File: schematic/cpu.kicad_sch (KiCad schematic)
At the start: 3 parts, among them U1 Z80CPU

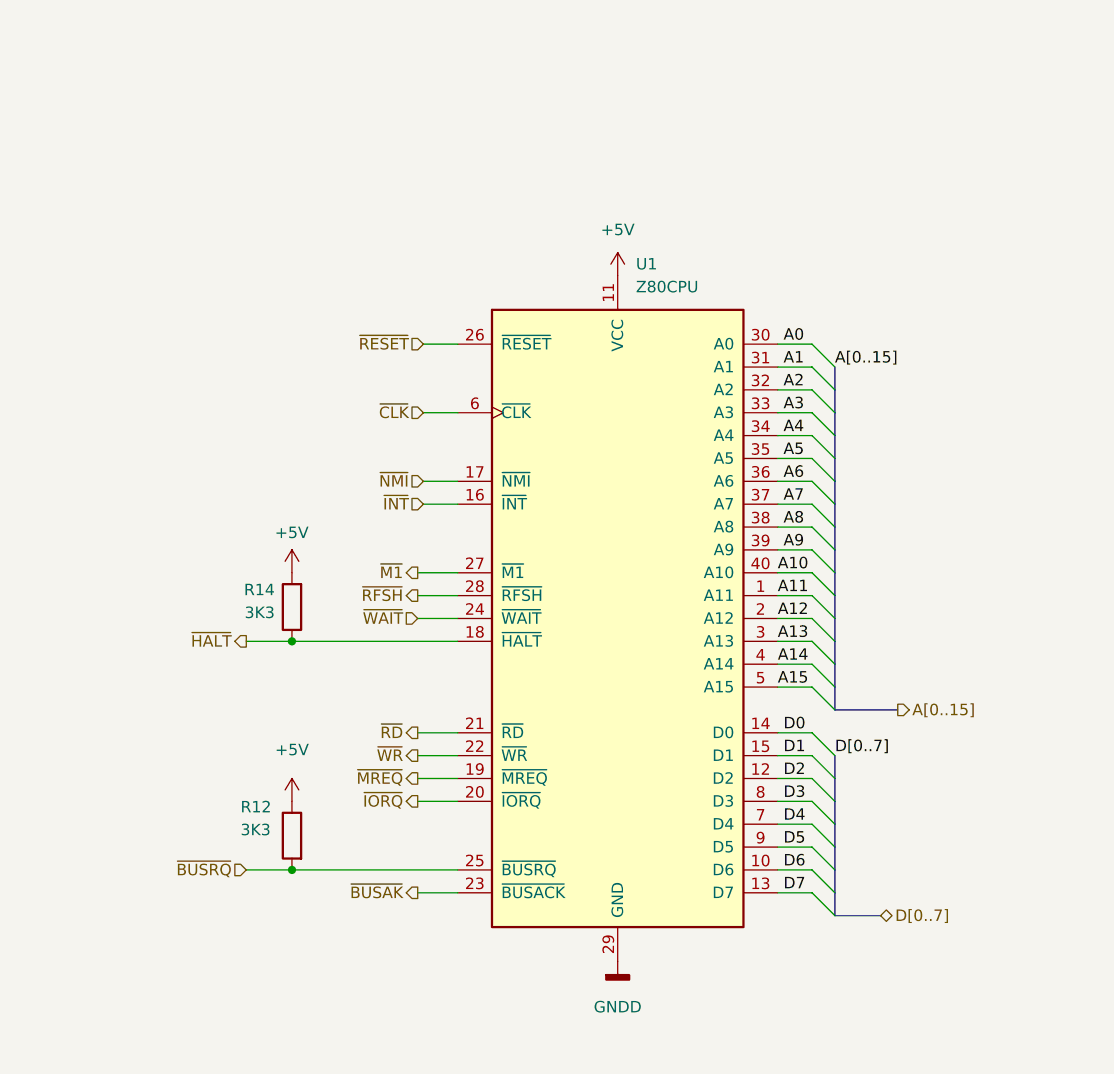
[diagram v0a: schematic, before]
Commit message: first commit of portable coleco, major changes... pcb meh. CPLD code tested, quartus build works.
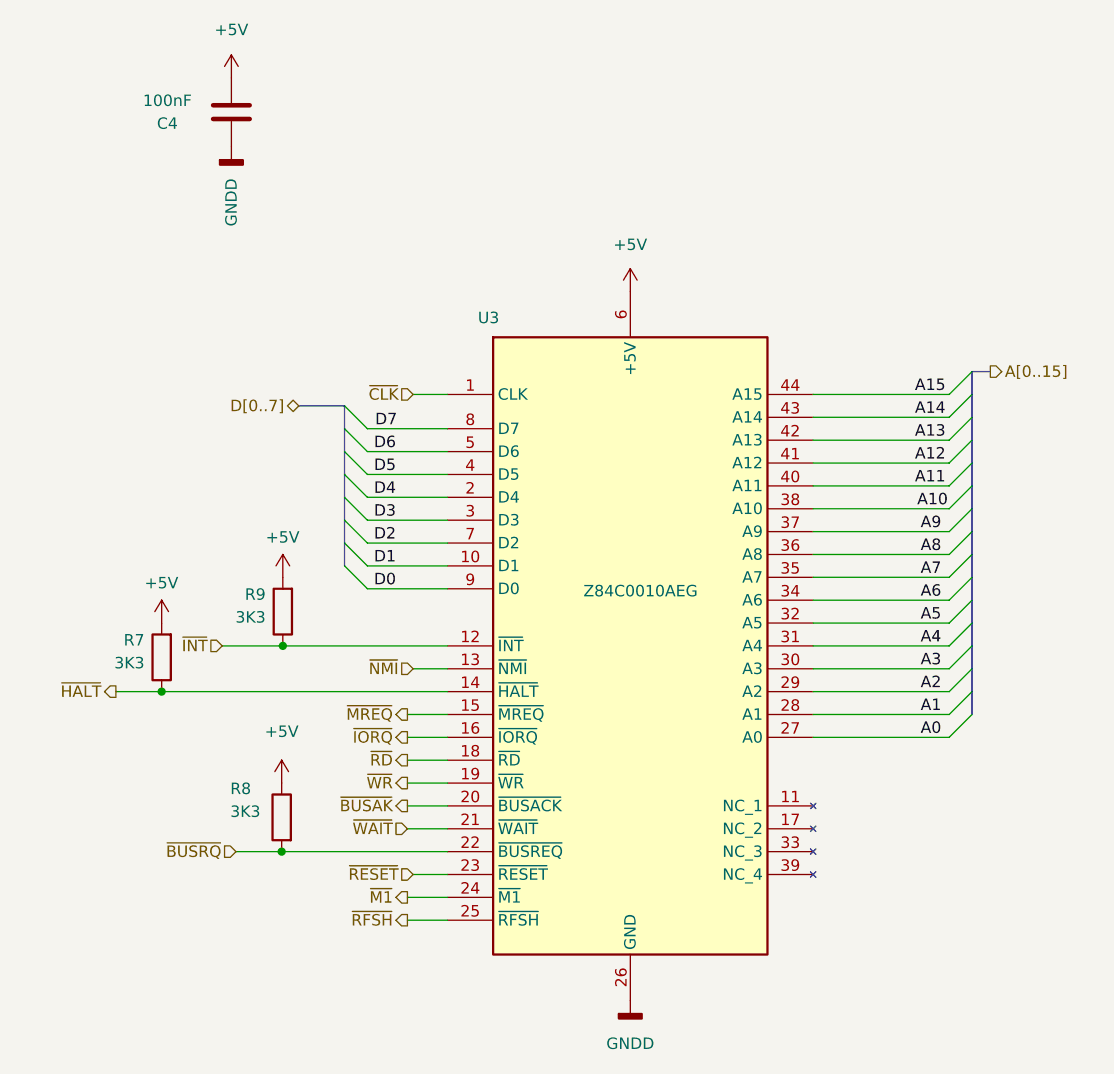
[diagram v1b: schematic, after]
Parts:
- removed U1: Z80CPU, Package_DIP:DIP-40_W15.24mm_LongPads, symbol CPU:Z80CPU
- added C4: 100nF, Capacitor_THT:C_Disc_D7.0mm_W2.5mm_P5.00mm, symbol Device:C
- added R9: 3K3, Resistor_THT:R_Axial_DIN0207_L6.3mm_D2.5mm_P10.16mm_Horizontal, symbol Device:R
- added U3: Z84C0010AEG, Package_QFP:LQFP-44_10x10mm_P0.8mm, symbol CPU_EXT:Z84C0010AEG
- renumbered R14 to R7, R12 to R8
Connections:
- net +5V: now also C4.1, R9.2, U3.6 (+5V)
- net A0: now also U3.27 (A0)
- net A1: now also U3.28 (A1)
- net A10: now also U3.38 (A10)
- net A11: now also U3.40 (A11)
- net A12: now also U3.41 (A12)
- net A13: now also U3.42 (A13)
- net A14: now also U3.43 (A14)
- net A15: now also U3.44 (A15)
- net A2: now also U3.29 (A2)
- net A3: now also U3.30 (A3)
- net A4: now also U3.31 (A4)
- net A5: now also U3.32 (A5)
- net A6: now also U3.34 (A6)
- net A7: now also U3.35 (A7)
- net A8: now also U3.36 (A8)
- net A9: now also U3.37 (A9)
- net D0: now also U3.9 (D0)
- net D1: now also U3.10 (D1)
- net D2: now also U3.7 (D2)
- net D3: now also U3.3 (D3)
- net D4: now also U3.2 (D4)
- net D5: now also U3.4 (D5)
- net D6: now also U3.5 (D6)
- net D7: now also U3.8 (D7)
- net GNDD: now also C4.2, U3.26 (GND)
- net ~{BUSAK}: now also U3.20 (~{BUSACK})
- net ~{BUSRQ}: now also U3.22 (~{BUSREQ})
- net ~{CLK}: now also U3.1 (CLK)
- net ~{HALT}: now also U3.14 (~{HALT})
- net ~{INT}: now also R9.1, U3.12 (~{INT})
- net ~{IORQ}: now also U3.16 (~{IORQ})
- net ~{M1}: now also U3.24 (~{M1})
- net ~{MREQ}: now also U3.15 (~{MREQ})
- net ~{NMI}: now also U3.13 (~{NMI})
- net ~{RD}: now also U3.18 (~{RD})
- net ~{RESET}: now also U3.23 (~{RESET})
- net ~{RFSH}: now also U3.25 (~{RFSH})
- net ~{WAIT}: now also U3.21 (~{WAIT})
- net ~{WR}: now also U3.19 (~{WR})
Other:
- moved on the sheet: R7, R8

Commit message: first prototype board complete with smd ram
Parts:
- C4: footprint Capacitor_THT:C_Disc_D7.0mm_W2.5mm_P5.00mm -> Capacitor_SMD:C_1206_3216Metric
- R7, R8, R9: footprint Resistor_THT:R_Axial_DIN0207_L6.3mm_D2.5mm_P10.16mm_Horizontal -> Resistor_SMD:R_0805_2012Metric
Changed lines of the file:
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@@
       (effects (font (size 1.27 1.27)) (justify right))
     )
-    (property "Footprint" "Resistor_THT:R_Axial_DIN0207_L6.3mm_D2.5mm_P10.16mm_Horizontal" (at 104.14 116.078 90)
+    (property "Footprint" "Resistor_SMD:R_0805_2012Metric" (at 104.14 116.078 90)
       (effects (font (size 1.27 1.27)) hide)
     )
@@
       (effects (font (size 1.27 1.27)))
     )
-    (property "Footprint" "Capacitor_THT:C_Disc_D7.0mm_W2.5mm_P5.00mm" (at 97.7392 41.529 0)
+    (property "Footprint" "Capacitor_SMD:C_1206_3216Metric" (at 97.7392 41.529 0)
       (effects (font (size 1.27 1.27)) hide)
     )
@@
       (effects (font (size 1.27 1.27)) (justify left))
     )
-    (property "Footprint" "Resistor_THT:R_Axial_DIN0207_L6.3mm_D2.5mm_P10.16mm_Horizontal" (at 90.805 98.298 90)
+    (property "Footprint" "Resistor_SMD:R_0805_2012Metric" (at 90.805 98.298 90)
       (effects (font (size 1.27 1.27)) hide)
     )
@@
       (effects (font (size 1.27 1.27)) (justify left))
     )
-    (property "Footprint" "Resistor_THT:R_Axial_DIN0207_L6.3mm_D2.5mm_P10.16mm_Horizontal" (at 104.267 93.218 90)
-      (effects (font (size 1.27 1.27)) hide)
-    )
+    (property "Footprint" "Resistor_SMD:R_0805_2012Metric" (at 104.267 93.218 90)
+      (effects (font (size 1.27 1.27)) hide)
+    )

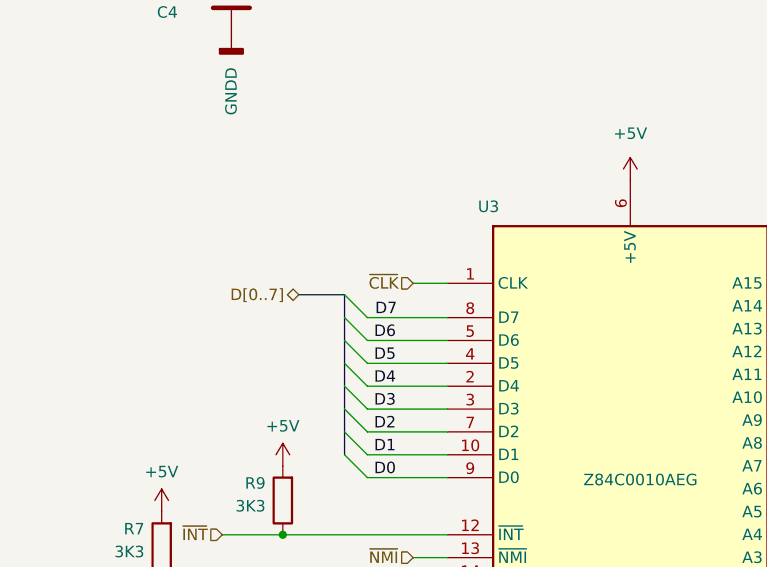
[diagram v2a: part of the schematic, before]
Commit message: added power port for lcd and adjusted board traces and fill
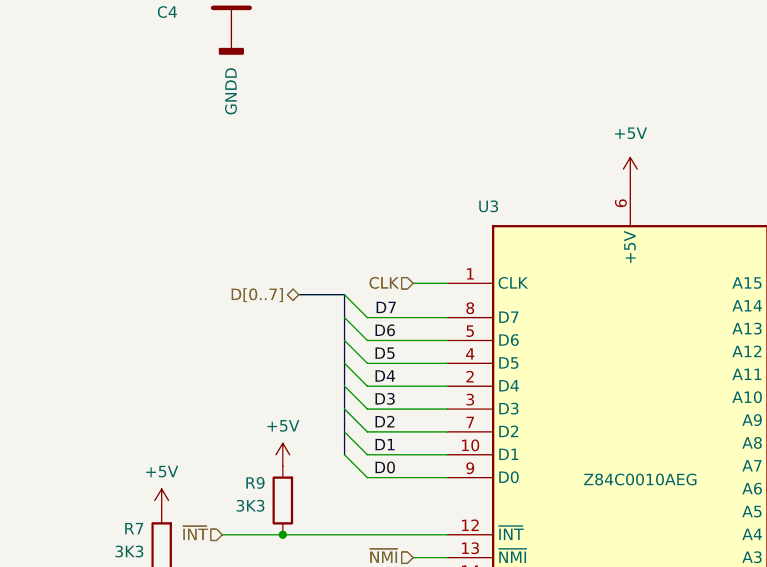
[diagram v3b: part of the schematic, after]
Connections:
- net ~{CLK} renamed CLK
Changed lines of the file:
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@@
     (effects (font (size 1.27 1.27)) (justify left))
   )
-  (hierarchical_label "~{CLK}" (shape input) (at 116.967 69.088 180) (fields_autoplaced)
+  (hierarchical_label "CLK" (shape input) (at 116.967 69.088 180) (fields_autoplaced)
     (effects (font (size 1.27 1.27)) (justify right))
   )

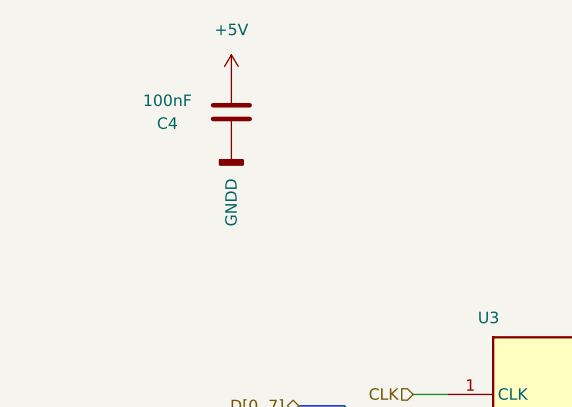
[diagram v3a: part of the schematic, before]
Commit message: first version with roller controller compat
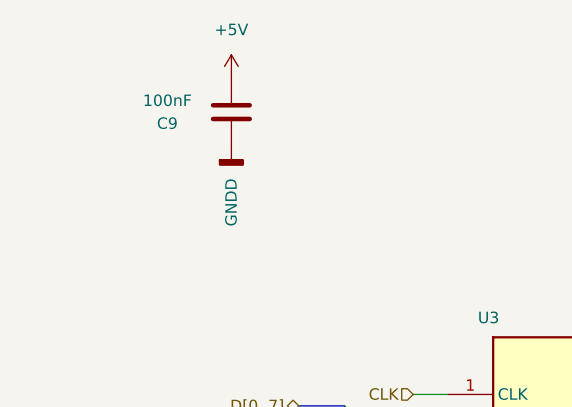
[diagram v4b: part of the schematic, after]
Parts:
- renumbered C4 to C9
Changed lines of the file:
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@@
   (symbol (lib_id "power:+5V") (at 96.774 33.909 0) (unit 1)
     (in_bom yes) (on_board yes) (dnp no) (fields_autoplaced)
-    (property "Reference" "#PWR021" (at 96.774 37.719 0)
+    (property "Reference" "#PWR018" (at 96.774 37.719 0)
       (effects (font (size 1.27 1.27)) hide)
     )
@@
     (instances
       (project "coleco_original"
-        (path "/970e0f64-111f-41e3-9f5a-fb0d0f6fa101/00000000-0000-0000-0000-00006262cd34"
-          (reference "#PWR021") (unit 1)
-        )
         (path "/970e0f64-111f-41e3-9f5a-fb0d0f6fa101/00000000-0000-0000-0000-00006262471e"
           (reference "#PWR018") (unit 1)
@@
   (symbol (lib_id "power:GNDD") (at 96.774 41.529 0) (unit 1)
     (in_bom yes) (on_board yes) (dnp no)
-    (property "Reference" "#PWR022" (at 96.774 47.879 0)
+    (property "Reference" "#PWR019" (at 96.774 47.879 0)
       (effects (font (size 1.27 1.27)) hide)
     )
@@
     (instances
       (project "coleco_original"
-        (path "/970e0f64-111f-41e3-9f5a-fb0d0f6fa101/00000000-0000-0000-0000-00006262cd34"
-          (reference "#PWR022") (unit 1)
-        )
         (path "/970e0f64-111f-41e3-9f5a-fb0d0f6fa101/00000000-0000-0000-0000-00006262471e"
           (reference "#PWR019") (unit 1)
@@
   (symbol (lib_id "Device:C") (at 96.774 37.719 0) (unit 1)
     (in_bom yes) (on_board yes) (dnp no)
-    (property "Reference" "C4" (at 89.662 38.989 0)
+    (property "Reference" "C9" (at 89.662 38.989 0)
       (effects (font (size 1.27 1.27)))
     )
@@
     (instances
       (project "coleco_original"
-        (path "/970e0f64-111f-41e3-9f5a-fb0d0f6fa101/00000000-0000-0000-0000-00006262cd34"
-          (reference "C4") (unit 1)
-        )
         (path "/970e0f64-111f-41e3-9f5a-fb0d0f6fa101/00000000-0000-0000-0000-00006262471e"
           (reference "C9") (unit 1)

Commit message: update pdf schematic and schematic wording
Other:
- title: Righteous Tentacle, Colecovision Reverse Engineering Project -> Mini Colecovision
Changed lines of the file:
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@@
   (paper "USLetter")
   (title_block
-    (title "Righteous Tentacle, Colecovision Reverse Engineering Project")
-    (date "2023-06-18")
-    (rev "1.0.0.F")
+    (title "Mini Colecovision")
+    (date "2024-03-25")
+    (rev "1.0.0")
     (company "sparkletron")
     (comment 1 "Jay Convertino")
     (comment 2 "MIT LICENSE")
-    (comment 3 "PCB: 75743 REV F")
+    (comment 3 "TARGET: Portable")
   )
   (junction (at 89.027 102.108) (diameter 0) (color 0 0 0 0)
